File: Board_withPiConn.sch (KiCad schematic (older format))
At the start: 66 parts, among them J1 Motor in, J2 220V IN, J3 Motor out, K1 PE014005, Q1 MPSA42, Q10 MPSA42, Q11 MPSA42, Q12 MPSA42, Q2 MPSA42, Q3 MPSA42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

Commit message: Fixed relay board
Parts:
- removed R3: 100k, symbol R
- J2: value 220V IN -> 230V IN
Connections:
- net +BATT: no longer Q5.3 (C)
- net at D1.2 (A), K1.1: now also Q5.3 (C)
- new net: D16.1 (K), D2.1 (K), D23.1 (K), D9.1 (K), R4.1
- new net: D2.2 (A), D3.2 (A), D4.2 (A), D5.2 (A), D6.2 (A), D7.2 (A), D8.2 (A), Q1.1 (E)
- new net: D10.2 (A), D11.2 (A), D12.2 (A), D13.2 (A), D14.2 (A), D15.2 (A), D9.2 (A), Q2.1 (E)
- new net: D16.2 (A), D17.2 (A), D18.2 (A), D19.2 (A), D20.2 (A), D21.2 (A), D22.2 (A), Q3.1 (E)
- new net: D23.2 (A), D24.2 (A), D25.2 (A), D26.2 (A), D27.2 (A), D28.2 (A), D29.2 (A), Q4.1 (E)
- new net: D15.1 (K), D22.1 (K), D29.1 (K), D8.1 (K), R10.1
- new net: D14.1 (K), D21.1 (K), D28.1 (K), D7.1 (K), R9.1
- new net: D13.1 (K), D20.1 (K), D27.1 (K), D6.1 (K), R8.1
- new net: D12.1 (K), D19.1 (K), D26.1 (K), D5.1 (K), R7.1
- new net: D11.1 (K), D18.1 (K), D25.1 (K), D4.1 (K), R6.1
- new net: D10.1 (K), D17.1 (K), D24.1 (K), D3.1 (K), R5.1
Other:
- moved on the sheet: D1, D10, D11, D12, D13, D14, D15, D16, D17, D18, D19, D2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
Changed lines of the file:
@@
 F 3 "~" H 7750 2350 60  0000 C CNN
 	1    7750 2350
-	0    1    1    0
+	0    -1   -1   0
 $EndComp
 $Comp
@@
 F 3 "~" H 7750 2950 60  0000 C CNN
 	1    7750 2950
-	0    1    1    0
+	0    -1   -1   0
 $EndComp
 $Comp
@@
 F 3 "~" H 7750 3450 60  0000 C CNN
 	1    7750 3450
-	0    1    1    0
+	0    -1   -1   0
 $EndComp
 $Comp
@@
 F 3 "~" H 7750 4050 60  0000 C CNN
 	1    7750 4050
-	0    1    1    0
+	0    -1   -1   0
 $EndComp
 $Comp
@@
 F 3 "~" H 10900 4050 60  0000 C CNN
 	1    10900 4050
-	0    1    1    0
+	0    -1   -1   0
 $EndComp
 $Comp
@@
 F 3 "~" H 10900 3450 60  0000 C CNN
 	1    10900 3450
-	0    1    1    0
+	0    -1   -1   0
 $EndComp
 $Comp
@@
 F 3 "~" H 10900 2950 60  0000 C CNN
 	1    10900 2950
-	0    1    1    0
+	0    -1   -1   0
 $EndComp
 $Comp
@@
 F 3 "~" H 10900 2350 60  0000 C CNN
 	1    10900 2350
-	0    1    1    0
+	0    -1   -1   0
 $EndComp
 $Comp
@@
 F 3 "~" H 10350 4050 60  0000 C CNN
 	1    10350 4050
-	0    1    1    0
+	0    -1   -1   0
 $EndComp
 $Comp
@@
 F 3 "~" H 10350 3450 60  0000 C CNN
 	1    10350 3450
-	0    1    1    0
+	0    -1   -1   0
 $EndComp
 $Comp
@@
 F 3 "~" H 10350 2950 60  0000 C CNN
 	1    10350 2950
-	0    1    1    0
+	0    -1   -1   0
 $EndComp
 $Comp
@@
 F 3 "~" H 10350 2350 60  0000 C CNN
 	1    10350 2350
-	0    1    1    0
+	0    -1   -1   0
 $EndComp
 $Comp
@@
 F 3 "~" H 9850 4050 60  0000 C CNN
 	1    9850 4050
-	0    1    1    0
+	0    -1   -1   0
 $EndComp
 $Comp
@@
 F 3 "~" H 9850 3450 60  0000 C CNN
 	1    9850 3450
-	0    1    1    0
+	0    -1   -1   0
 $EndComp
 $Comp
@@
 F 3 "~" H 9850 2950 60  0000 C CNN
 	1    9850 2950
-	0    1    1    0
+	0    -1   -1   0
 $EndComp
 $Comp
@@
 F 3 "~" H 9850 2350 60  0000 C CNN
 	1    9850 2350
-	0    1    1    0
+	0    -1   -1   0
 $EndComp
 $Comp
@@
 F 3 "~" H 9350 4050 60  0000 C CNN
 	1    9350 4050
-	0    1    1    0
+	0    -1   -1   0
 $EndComp
 $Comp
@@
 F 3 "~" H 9350 3450 60  0000 C CNN
 	1    9350 3450
-	0    1    1    0
+	0    -1   -1   0
 $EndComp
 $Comp
@@
 F 3 "~" H 9350 2950 60  0000 C CNN
 	1    9350 2950
-	0    1    1    0
+	0    -1   -1   0
 $EndComp
 $Comp
@@
 F 3 "~" H 9350 2350 60  0000 C CNN
 	1    9350 2350
-	0    1    1    0
+	0    -1   -1   0
 $EndComp
 $Comp
@@
 F 3 "~" H 8800 4050 60  0000 C CNN
 	1    8800 4050
-	0    1    1    0
+	0    -1   -1   0
 $EndComp
 $Comp
@@
 F 3 "~" H 8800 3450 60  0000 C CNN
 	1    8800 3450
-	0    1    1    0
+	0    -1   -1   0
 $EndComp
 $Comp
@@
 F 3 "~" H 8800 2950 60  0000 C CNN
 	1    8800 2950
-	0    1    1    0
+	0    -1   -1   0
 $EndComp
 $Comp
@@
 F 3 "~" H 8800 2350 60  0000 C CNN
 	1    8800 2350
-	0    1    1    0
+	0    -1   -1   0
 $EndComp
 $Comp
@@
 F 3 "~" H 8300 4050 60  0000 C CNN
 	1    8300 4050
-	0    1    1    0
+	0    -1   -1   0
 $EndComp
 $Comp
@@
 F 3 "~" H 8300 3450 60  0000 C CNN
 	1    8300 3450
-	0    1    1    0
+	0    -1   -1   0
 $EndComp
 $Comp
@@
 F 3 "~" H 8300 2950 60  0000 C CNN
 	1    8300 2950
-	0    1    1    0
+	0    -1   -1   0
 $EndComp
 $Comp
@@
 F 3 "~" H 8300 2350 60  0000 C CNN
 	1    8300 2350
-	0    1    1    0
+	0    -1   -1   0
 $EndComp
 $Comp
@@
 L D D1
 U 1 1 5A8C7954
-P 4150 2100
-F 0 "D1" H 4150 2200 50  0000 C CNN
-F 1 "D1" H 4150 2000 50  0000 C CNN
-F 2 "" H 4150 2100 50  0001 C CNN
-F 3 "" H 4150 2100 50  0001 C CNN
-	1    4150 2100
-	1    0    0    -1
+P 3900 1800
+F 0 "D1" H 3900 1900 50  0000 C CNN
+F 1 "D1" H 3900 1700 50  0000 C CNN
+F 2 "" H 3900 1800 50  0001 C CNN
+F 3 "" H 3900 1800 50  0001 C CNN
+	1    3900 1800
+	0    1    1    0
 $EndComp
 $Comp
@@
 P 4500 2350
 F 0 "J2" H 4500 2450 50  0000 C CNN
-F 1 "220V IN" H 4500 2250 50  0000 C CNN
+F 1 "230V IN" H 4500 2250 50  0000 C CNN
 F 2 "" H 4500 2350 50  0001 C CNN
 F 3 "" H 4500 2350 50  0001 C CNN
@@
 	0    1    1    0
 $EndComp
-$Comp
-L R R3
-U 1 1 5A8A5493
-P 3250 3350
-F 0 "R3" V 3330 3350 50  0000 C CNN
-F 1 "100k" V 3250 3350 50  0000 C CNN
-F 2 "" V 3180 3350 50  0001 C CNN
-F 3 "" H 3250 3350 50  0001 C CNN
-	1    3250 3350
-	1    0    0    -1
-$EndComp
 Wire Wire Line
 	1550 1200 1550 1700
@@
 	3900 3250 3900 5750
 Wire Wire Line
-	3550 1500 4300 1500
-Connection ~ 3900 1500
-Wire Wire Line
-	3900 2100 4000 2100
+	3550 2100 4300 2100
 Connection ~ 3900 2100
-Wire Wire Line
-	3900 1200 3900 2100
-Wire Wire Line
-	3550 1500 3550 2850
 Wire Wire Line
 	3550 2850 3900 2850
@@
 Wire Wire Line
 	3300 3200 3300 3050
-Wire Wire Line
-	3250 3500 3900 3500
-Connection ~ 3900 3500
 Connection ~ 3900 5750
 $Comp
@@
 	1    0    0    -1
 $EndComp
+Wire Wire Line
+	4300 1500 3900 1500
+Wire Wire Line
+	3900 1200 3900 1650
+Wire Wire Line
+	3550 2850 3550 2100
+Wire Wire Line
+	3900 2100 3900 1950
+Connection ~ 3900 1500
 $EndSCHEMATC

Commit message: fixed relay board
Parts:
- added R1337: 100k, symbol R
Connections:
- net GND: now also R1337.2
- net at R2.2, U1.27 ((ADC4/SDA)PC4): now also R1337.1
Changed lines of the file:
@@
 	2400 3200 3300 3200
 Wire Wire Line
-	3300 3200 3300 3050
+	3300 3050 3300 3300
 Connection ~ 3900 5750
 $Comp
@@
 	3900 2100 3900 1950
 Connection ~ 3900 1500
+$Comp
+L R R1337
+U 1 1 5A91025C
+P 3450 3300
+F 0 "R1337" V 3530 3300 50  0000 C CNN
+F 1 "100k" V 3450 3300 50  0000 C CNN
+F 2 "" V 3380 3300 50  0001 C CNN
+F 3 "" H 3450 3300 50  0001 C CNN
+	1    3450 3300
+	0    -1   -1   0
+$EndComp
+Connection ~ 3300 3200
+Wire Wire Line
+	3600 3300 3900 3300
+Connection ~ 3900 3300
 $EndSCHEMATC

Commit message: updated board layouts
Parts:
- D1: value D1 -> 1N4007
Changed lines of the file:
@@
 P 3900 1800
 F 0 "D1" H 3900 1900 50  0000 C CNN
-F 1 "D1" H 3900 1700 50  0000 C CNN
+F 1 "1N4007" H 3900 1700 50  0000 C CNN
 F 2 "" H 3900 1800 50  0001 C CNN
 F 3 "" H 3900 1800 50  0001 C CNN

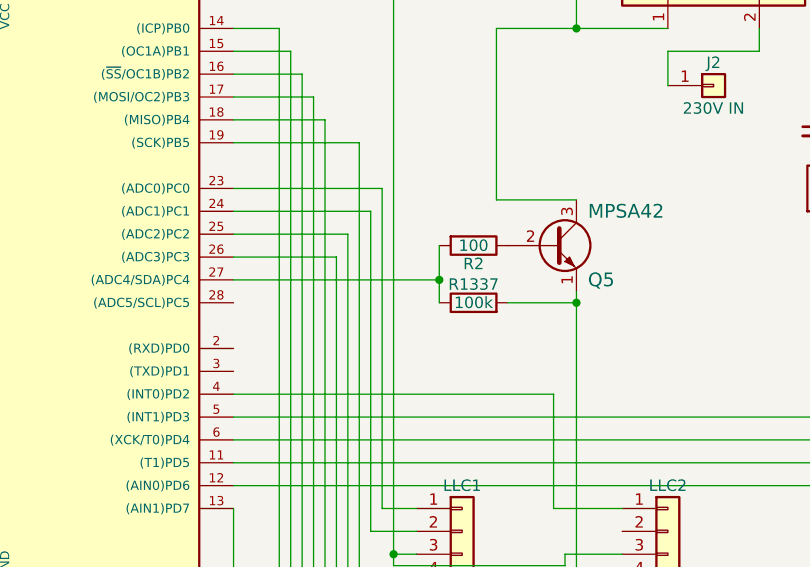
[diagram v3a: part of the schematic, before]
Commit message: fixed bug in extension board
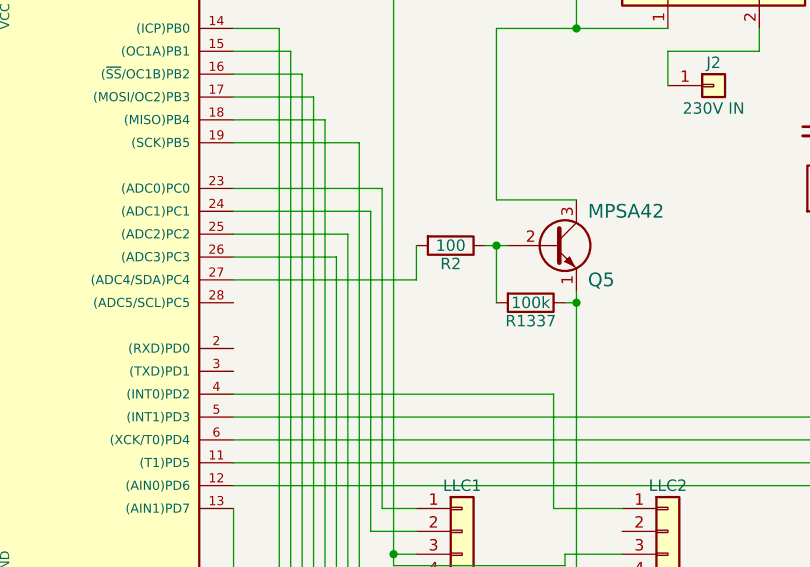
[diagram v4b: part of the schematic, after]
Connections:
- net GND: now also R1337.1; no longer R1337.2
- net at R2.2, U1.27 ((ADC4/SDA)PC4): no longer R1337.1
- net at Q5.2 (B), R2.1: now also R1337.2
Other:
- moved on the sheet: R1337, R2
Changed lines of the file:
@@
 L R R2
 U 1 1 5A8B7F49
-P 3450 3050
-F 0 "R2" V 3530 3050 50  0000 C CNN
-F 1 "100" V 3450 3050 50  0000 C CNN
-F 2 "" V 3380 3050 50  0001 C CNN
-F 3 "" H 3450 3050 50  0001 C CNN
-	1    3450 3050
+P 3350 3050
+F 0 "R2" V 3430 3050 50  0000 C CNN
+F 1 "100" V 3350 3050 50  0000 C CNN
+F 2 "" V 3280 3050 50  0001 C CNN
+F 3 "" H 3350 3050 50  0001 C CNN
+	1    3350 3050
 	0    1    1    0
 $EndComp
@@
 Wire Wire Line
 	4700 2200 4700 2100
-Wire Wire Line
-	2400 3200 3300 3200
-Wire Wire Line
-	3300 3050 3300 3300
 Connection ~ 3900 5750
 $Comp
@@
 L R R1337
 U 1 1 5A91025C
-P 3450 3300
-F 0 "R1337" V 3530 3300 50  0000 C CNN
-F 1 "100k" V 3450 3300 50  0000 C CNN
-F 2 "" V 3380 3300 50  0001 C CNN
-F 3 "" H 3450 3300 50  0001 C CNN
-	1    3450 3300
-	0    -1   -1   0
+P 3700 3300
+F 0 "R1337" V 3780 3300 50  0000 C CNN
+F 1 "100k" V 3700 3300 50  0000 C CNN
+F 2 "" V 3630 3300 50  0001 C CNN
+F 3 "" H 3700 3300 50  0001 C CNN
+	1    3700 3300
+	0    1    1    0
 $EndComp
-Connection ~ 3300 3200
-Wire Wire Line
-	3600 3300 3900 3300
 Connection ~ 3900 3300
+Wire Wire Line
+	3550 3300 3550 3050
+Wire Wire Line
+	3500 3050 3600 3050
+Connection ~ 3550 3050
+Wire Wire Line
+	3850 3300 3900 3300
+Wire Wire Line
+	3200 3050 3200 3200
+Wire Wire Line
+	3200 3200 2400 3200
 $EndSCHEMATC
